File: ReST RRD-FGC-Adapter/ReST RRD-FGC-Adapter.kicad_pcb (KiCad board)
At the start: 2 copper layers, 28.8 x 43.5 mm, 40 parts, among them P1 CONN_02X05, P2 CONN_02X05, P3 CONN_02X05, P4 CONN_02X05, Q1 BSS138, Q2 BSS138, Q3 BSS138, Q4 BSS138, U1 MIC5205

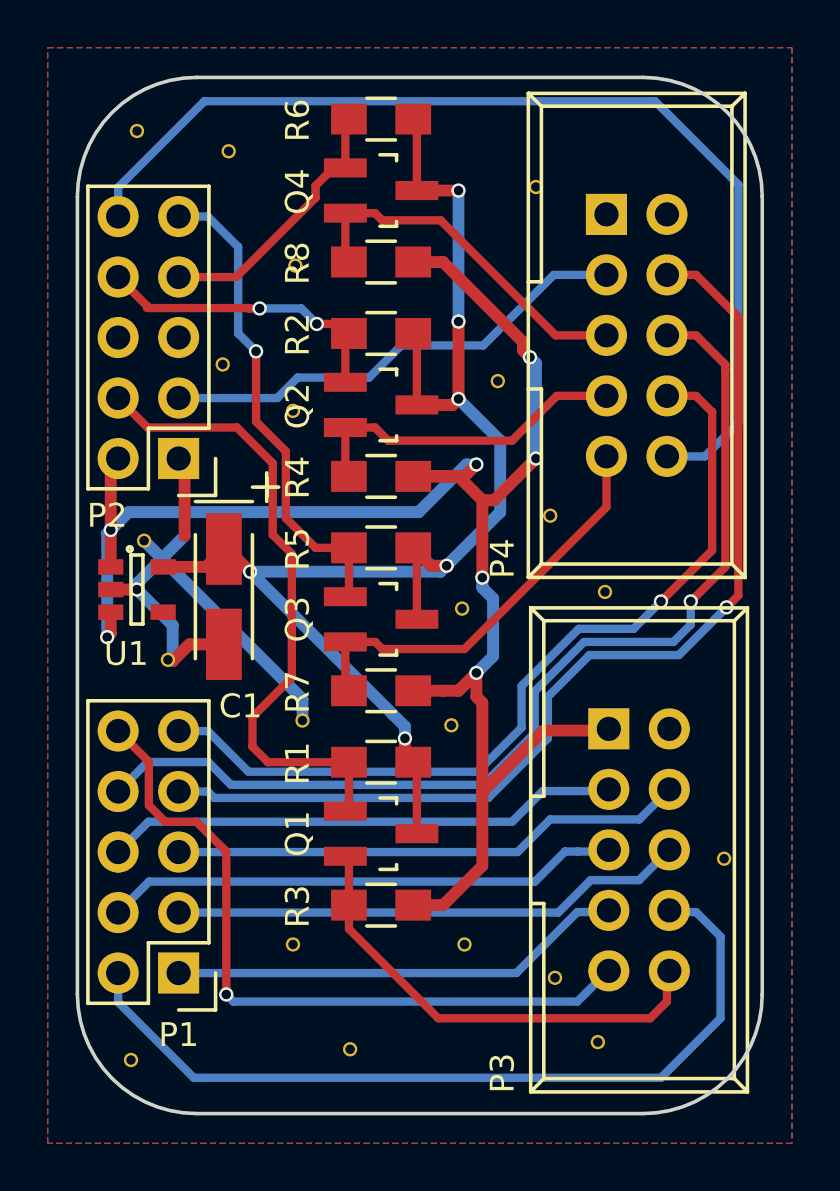
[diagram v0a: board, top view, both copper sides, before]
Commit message: forgot naming of the connector in the lcd adapter
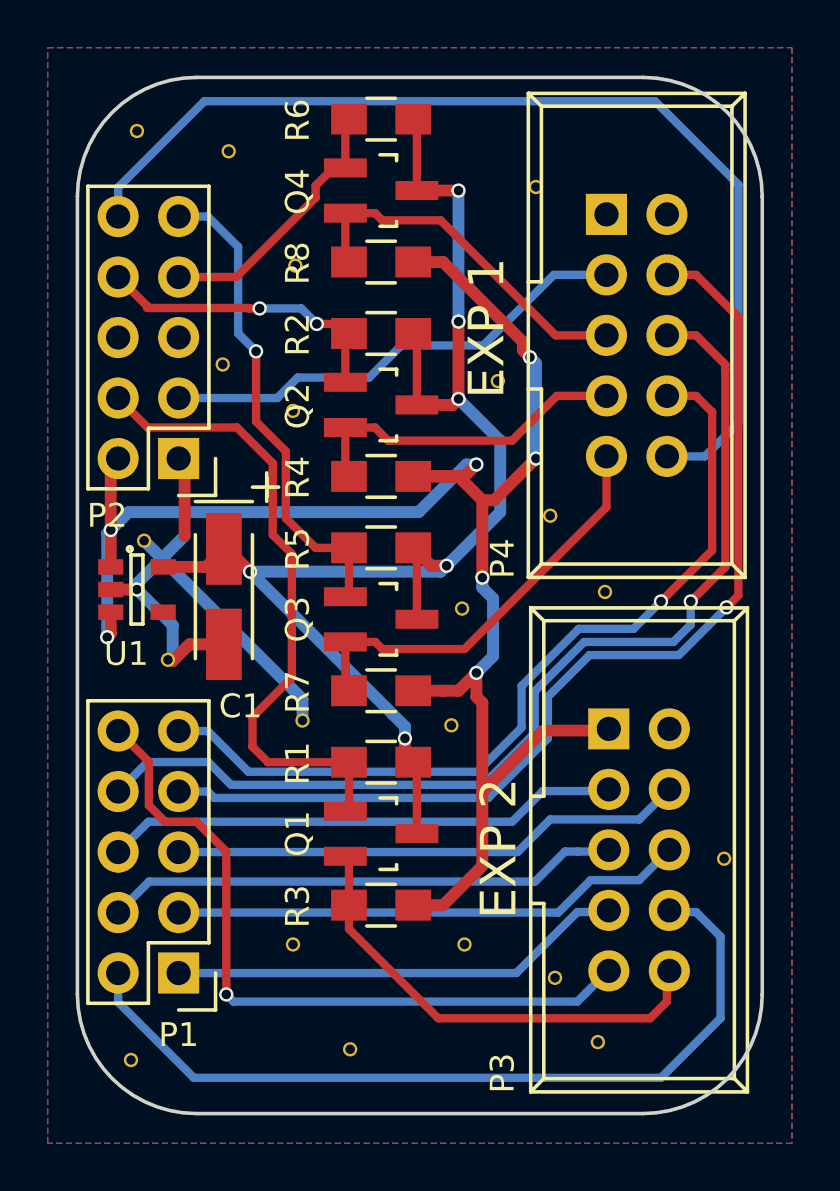
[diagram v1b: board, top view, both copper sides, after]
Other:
- board text added: "EXP 1"
- board text added: "EXP 2"
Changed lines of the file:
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@@
 (kicad_pcb (version 4) (host pcbnew 4.0.2-stable)
   (general
-    (links 0)
+    (links 68)
     (no_connects 0)
     (area 104.5 116.525 135.750001 162.750001)
     (thickness 1.6)
-    (drawings 9)
+    (drawings 11)
     (tracks 264)
     (zones 0)
@@
       (layerselection 0x010f0_80000001)
       (usegerberextensions true)
-      (excludeedgelayer true)
-      (linewidth 0.300000)
+      (excludeedgelayer false)
+      (linewidth 0.100000)
       (plotframeref false)
       (viasonmask false)
@@
       (psa4output false)
       (plotreference true)
-      (plotvalue true)
+      (plotvalue false)
       (plotinvisibletext false)
       (padsonsilk false)
@@
       (xy -1.51384 -2.24536)) (layer B.SilkS) (width 0.00254))
   )
+  (gr_text "EXP 2" (at 123.444 150.368 90) (layer F.SilkS)
+    (effects (font (size 1.5 1.5) (thickness 0.3)))
+  )
+  (gr_text "EXP 1" (at 122.936 128.524 90) (layer F.SilkS)
+    (effects (font (size 1.5 1.5) (thickness 0.3)))
+  )
   (gr_text "ReST32 LCD Adapter for\nRepRapDiscount Full Graphic\nSmart Controller" (at 119.75 141 90) (layer B.SilkS)
